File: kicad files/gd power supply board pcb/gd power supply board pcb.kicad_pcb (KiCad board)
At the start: 2 copper layers, 86.9 x 40.1 mm, 129 parts, among them J1 15V_IN, J2 15V_IN, J3 Edge Connector, Q1 FDS9435A, Q2 BC817, Q3 MMBT3906, Q4 FDS9435A, U1 MAX17580, U2 mc34063, U3 TPS563240DDCR, U4 TPS563240DDCR

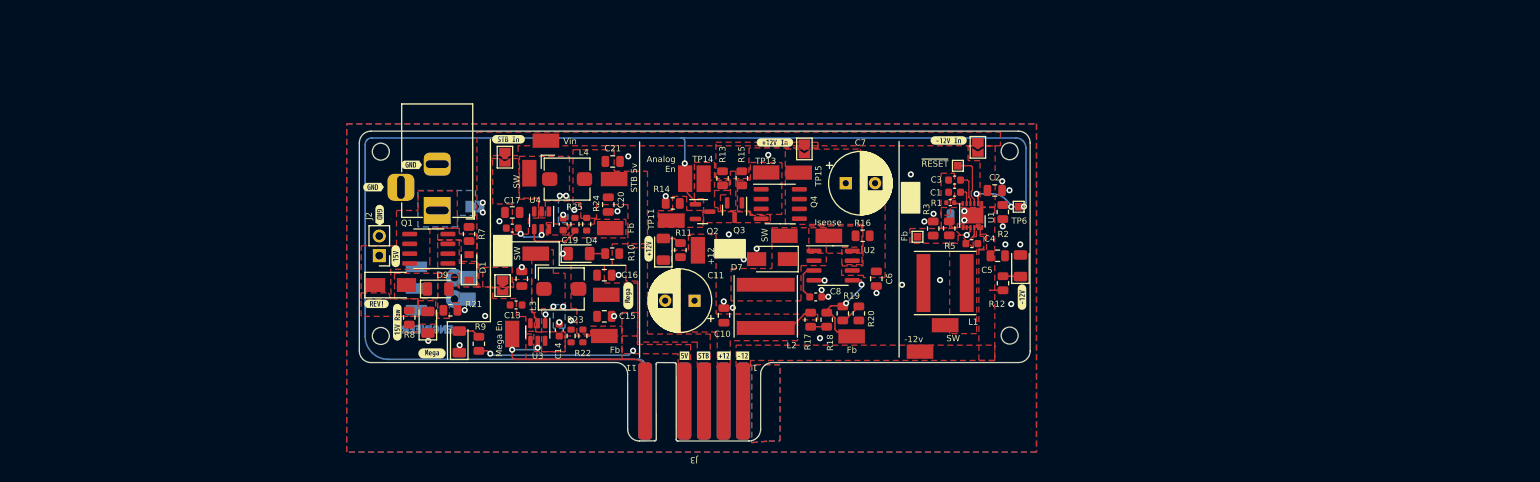
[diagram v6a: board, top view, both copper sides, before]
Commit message: added filters and ripped up the board
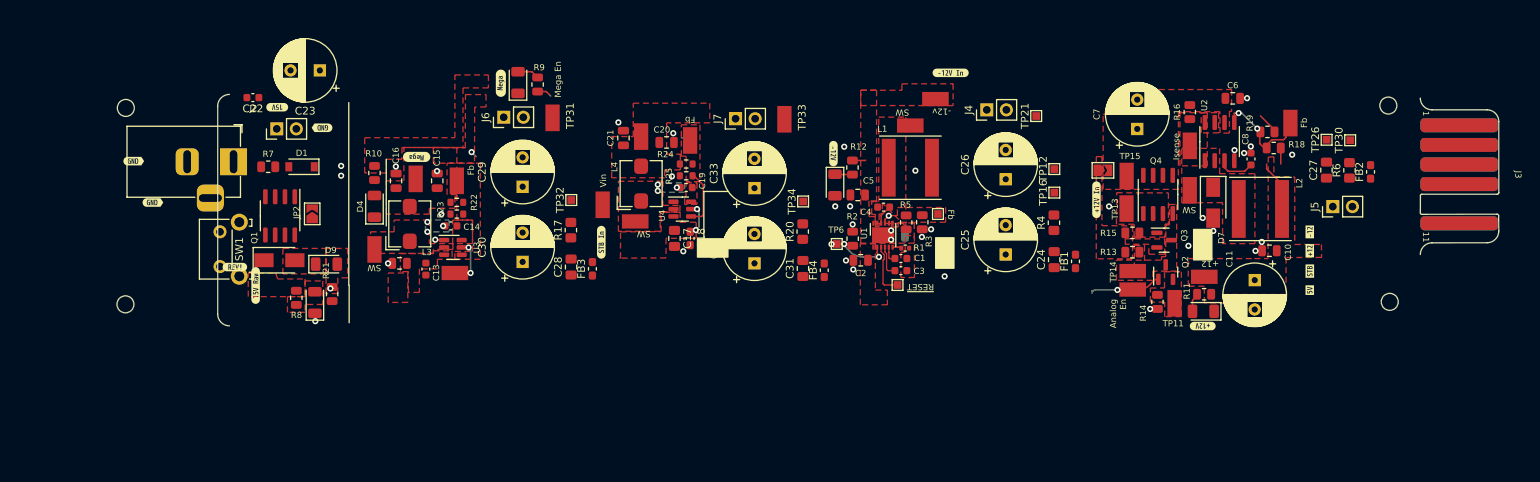
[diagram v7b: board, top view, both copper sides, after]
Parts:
- removed JP3: neg_12_jmp, Jumper:SolderJumper-2_P1.3mm_Open_TrianglePad1.0x1.5mm
- removed JP4: mega_5v_jmp, Jumper:SolderJumper-2_P1.3mm_Open_TrianglePad1.0x1.5mm
- removed JP5: stb_5v_jmp, Jumper:SolderJumper-2_P1.3mm_Open_TrianglePad1.0x1.5mm
- removed REF**: Polarity_Center_Positive_6mm_SilkScreen, Symbol:Polarity_Center_Positive_6mm_SilkScreen
- removed REF**: OSHW-Logo2_7.3x6mm_SilkScreen, Symbol:OSHW-Logo2_7.3x6mm_SilkScreen
- removed REF**: KiCad-Logo2_5mm_SilkScreen, Symbol:KiCad-Logo2_5mm_SilkScreen
- removed svg2mod: G***, My Libraries:BE10v2
- added C22: 1u, Capacitor_SMD:C_0603_1608Metric, F.Cu at (85.8, 74.5)
- added C23: 120u, Capacitor_THT:CP_Radial_D8.0mm_P3.80mm, F.Cu at (94.5, 71.0)
- added C24: Cdamp, Capacitor_SMD:C_0805_2012Metric_Pad1.18x1.45mm_HandSolder, F.Cu at (189.6, 95.5)
- added C25: 120u, Capacitor_THT:CP_Radial_D8.0mm_P3.80mm, F.Cu at (183.3, 94.9)
- added C26: 120u, Capacitor_THT:CP_Radial_D8.0mm_P3.80mm, F.Cu at (183.3, 85.1)
- added C27: Cdamp, Capacitor_SMD:C_0805_2012Metric_Pad1.18x1.45mm_HandSolder, F.Cu at (224.9, 83.9)
- added C28: Cdamp, Capacitor_SMD:C_0805_2012Metric_Pad1.18x1.45mm_HandSolder, F.Cu at (127.0, 96.5)
- added C29: 120u, Capacitor_THT:CP_Radial_D8.0mm_P3.80mm, F.Cu at (120.7, 86.1)
- added C30: 120u, Capacitor_THT:CP_Radial_D8.0mm_P3.80mm, F.Cu at (120.7, 95.8)
- added C31: Cdamp, Capacitor_SMD:C_0805_2012Metric_Pad1.18x1.45mm_HandSolder, F.Cu at (157.0, 96.7)
- added C32: 120u, Capacitor_THT:CP_Radial_D8.0mm_P3.80mm, F.Cu at (150.8, 96.0)
- added C33: 120u, Capacitor_THT:CP_Radial_D8.0mm_P3.80mm, F.Cu at (150.8, 86.3)
- added FB1: 220, Inductor_SMD:L_0603_1608Metric_Pad1.05x0.95mm_HandSolder, F.Cu at (192.3, 95.8)
- added FB2: 220, Inductor_SMD:L_0603_1608Metric_Pad1.05x0.95mm_HandSolder, F.Cu at (230.6, 84.2)
- added FB3: 220, Inductor_SMD:L_0603_1608Metric_Pad1.05x0.95mm_HandSolder, F.Cu at (129.8, 96.7)
- added FB4: 220, Inductor_SMD:L_0603_1608Metric_Pad1.05x0.95mm_HandSolder, F.Cu at (159.8, 96.9)
- added J4: -12v_vin, Connector_PinHeader_2.54mm:PinHeader_1x02_P2.54mm_Vertical, F.Cu at (180.9, 76.1)
- added J5: +12v_vin, Connector_PinHeader_2.54mm:PinHeader_1x02_P2.54mm_Vertical, F.Cu at (225.7, 88.7)
- added J6: mega_vin, Connector_PinHeader_2.54mm:PinHeader_1x02_P2.54mm_Vertical, F.Cu at (118.3, 77.1)
- added J7: stb_vin, Connector_PinHeader_2.54mm:PinHeader_1x02_P2.54mm_Vertical, F.Cu at (148.3, 77.3)
- added R4: Rdamp, Resistor_SMD:R_0805_2012Metric_Pad1.20x1.40mm_HandSolder, F.Cu at (189.6, 90.7)
- added R6: Rdamp, Resistor_SMD:R_0805_2012Metric_Pad1.20x1.40mm_HandSolder, F.Cu at (227.8, 84.0)
- added SW1: SW_SPST, Button_Switch_THT:SW_Tactile_SKHH_Angled, F.Cu at (81.5, 96.4)
- added TP12: TestPoint_Harwin, TestPoint:TestPoint_Pad_1.0x1.0mm, F.Cu at (189.6, 83.8)
- added TP16: TestPoint_Harwin, TestPoint:TestPoint_Pad_1.0x1.0mm, F.Cu at (189.6, 86.8)
- added TP21: TestPoint_Harwin, TestPoint:TestPoint_Pad_1.0x1.0mm, F.Cu at (187.3, 76.9)
- added TP26: TestPoint_Harwin, TestPoint:TestPoint_Pad_1.0x1.0mm, F.Cu at (224.9, 80.0)
- added TP30: TestPoint_Harwin, TestPoint:TestPoint_Pad_1.0x1.0mm, F.Cu at (227.9, 80.1)
- added TP31: TestPoint_Harwin, My Libraries:Harwin-S1751-46-Test-Point, F.Cu at (124.6, 77.2)
- added TP32: TestPoint_Harwin, TestPoint:TestPoint_Pad_1.0x1.0mm, F.Cu at (127.0, 87.8)
- added TP33: TestPoint_Harwin, My Libraries:Harwin-S1751-46-Test-Point, F.Cu at (154.6, 77.3)
- added TP34: TestPoint_Harwin, TestPoint:TestPoint_Pad_1.0x1.0mm, F.Cu at (157.1, 88.0)
- C17: footprint Capacitor_SMD:C_0805_2012Metric -> Capacitor_SMD:C_0805_2012Metric_Pad1.18x1.45mm_HandSolder
- C18: footprint Capacitor_SMD:C_0603_1608Metric -> Capacitor_SMD:C_0603_1608Metric_Pad1.08x0.95mm_HandSolder
- C6: value 100u -> 10u
- JP1: value 15V_Jmp -> Limit_Jmp
- JP2: moved to F.Cu
- R1: value R -> dnp
- R13: value 50k -> 47k
- R14: value 30k -> 33k
- R17, R20: value 0 -> Rdamp; footprint Resistor_SMD:R_0805_2012Metric -> Resistor_SMD:R_0805_2012Metric_Pad1.20x1.40mm_HandSolder
- moved J3 109.7 mm to (247.1, 84.5), turned to -90 degrees
- moved kibuzzard-62380FF5 81.4 mm to (222.7, 99.5), turned to 90 degrees
- moved kibuzzard-62381032 79.3 mm to (222.7, 97.0), turned to 90 degrees
- moved kibuzzard-6238106E 78.6 mm to (217.8, 102.0), turned to 180 degrees
- moved kibuzzard-62381000 77.1 mm to (222.7, 94.4), turned to 90 degrees
- moved kibuzzard-6238101E 75.2 mm to (222.7, 91.9), turned to 90 degrees
- moved C11 72.6 mm to (215.6, 98.2), turned to -90 degrees
- moved kibuzzard-62380E7D 72.5 mm to (208.8, 104.1), turned to 180 degrees
- moved C10 71.1 mm to (217.5, 94.4), turned to 0 degrees
- moved D5 70.4 mm to (208.9, 102.2), turned to 180 degrees
- moved R11 68.1 mm to (209.0, 100.0), turned to 0 degrees
- moved TP11 66.0 mm to (205.2, 101.2), turned to -90 degrees
- moved TP20 65.7 mm to (209.0, 97.7), turned to 180 degrees
- moved L2 65.3 mm to (216.3, 89.0), turned to 0 degrees
- moved R14 64.1 mm to (203.0, 101.0), turned to -90 degrees
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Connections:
- net Net-(C12-Pad1) renamed /mega5v/mega_Vin
- D8 pad 1: /15v_Raw -> /15V_SWd
- JP1 pad 1: /Vin -> /pos12/12v_Vin
- JP2 pad 1: /15v_Raw -> /15V_SWd
- Q1 pad 5: /15v_Raw -> /15V_SWd
- Q1 pad 6: /15v_Raw -> /15V_SWd
- Q1 pad 7: /15v_Raw -> /15V_SWd
- Q1 pad 8: /15v_Raw -> /15V_SWd
- Q3 pad 2: /Vin -> /pos12/12v_Vin
- R13 pad 1: /Vin -> /pos12/12v_Vin
- R15 pad 1: /Vin -> /pos12/12v_Vin
- R17 pad 1: /Pos12_Out -> GND
- R17 pad 2: Net-(R17-Pad2) -> Net-(C28-Pad2)
- R18 pad 1: Net-(R18-Pad1) -> Net-(TP19-Pad1)
- R18 pad 2: Net-(R17-Pad2) -> /Pos12_Out
- R19 pad 1: Net-(R18-Pad1) -> GND
- R19 pad 2: Net-(R19-Pad2) -> Net-(TP19-Pad1)
- R20 pad 2: Net-(R19-Pad2) -> Net-(C31-Pad2)
- R3 pad 1: GND -> /neg12/FB
- R3 pad 2: /neg12/FB -> GND
- R5 pad 1: /neg12/FB -> /Neg12_Out
- R5 pad 2: /Neg12_Out -> /neg12/FB
- R8 pad 2: /15v_Raw -> /15V_SWd
- TP19 pad 1: Net-(R18-Pad1) -> Net-(TP19-Pad1)
- U2 pad 5: Net-(R18-Pad1) -> Net-(TP19-Pad1)
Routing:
- net /Analog_En: track 180.4 -> 18.5 mm
- net /Mega_En: track 29.1 -> 6.32 mm
- net /mega_5v: track 20.5 -> 2.76 mm, vias 2 -> 1
- net Net-(TP19-Pad1): track 0.00 -> 16.5 mm, vias 0 -> 2
- net Net-(R18-Pad1): track 13.7 -> 0.00 mm, vias 2 -> 0
- net Net-(R19-Pad2): track 2.84 -> 0.00 mm
- net Net-(R17-Pad2): track 2.08 -> 0.00 mm
- net /Pos12_Out: track 6.64 -> 8.72 mm
- net Net-(D4-Pad2): track 2.01 -> 0.00 mm
- net GND: vias 39 -> 34
- removed copper zone on B.Cu, net /15v_Raw
- removed copper zone on B.Cu, net GND
- removed copper zone on F.Cu, net GND
- removed copper zone on F.Cu, net Net-(D1-Pad2)
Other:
- board size 86.9 x 40.1 mm -> 165.9 x 30 mm
- copper layers 2 -> 4
- board text removed: "STB 5v"

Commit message: rev2 - round 1
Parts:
- removed TP12, TP16, TP6: TestPoint_Harwin, TestPoint:TestPoint_Pad_1.0x1.0mm
- R2: value 10k -> 10K
- moved H3 89.9 mm to (143.4, 107.7)
- moved H2 89.6 mm to (143.6, 67.2)
- moved FB2 61.9 mm to (168.9, 90.0), turned to 0 degrees
- moved R6 58.2 mm to (170.5, 74.3), turned to -90 degrees
- moved J5 58.0 mm to (168.0, 82.9), turned to 0 degrees
- moved C27 54.7 mm to (170.4, 78.4)
- moved J4 43.5 mm to (143.9, 99.1)
- moved R4 42.7 mm to (148.4, 102.0), turned to 0 degrees
- moved FB4 42.1 mm to (121.7, 79.0), turned to -90 degrees
- moved FB1 41.7 mm to (150.7, 98.1), turned to 0 degrees
- moved R20 41.6 mm to (117.5, 78.9)
- moved C31 41.3 mm to (119.8, 78.9)
- moved TP34 40.4 mm to (116.8, 83.9), turned to 0 degrees
- moved C24 39.4 mm to (150.5, 100.0), turned to 180 degrees
- moved C26 37.4 mm to (146.9, 76.4), turned to 0 degrees
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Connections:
- net /neg12/FB renamed /neg12/-12v_FB
- net /pos12/SW renamed /pos12/+12V_SW
- net Net-(R24-Pad1) renamed /stb_5v/stb_FB
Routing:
- net /Analog_En: track 18.5 -> 0.00 mm, vias 4 -> 0
- net Net-(R18-Pad1): track 16.5 -> 4.17 mm, vias 2 -> 0
- net /Pos12_Out: track 8.72 -> 0.00 mm
- net GND: track 3.06 -> 0.00 mm, vias 34 -> 0
- net Net-(D3-Pad2): track 2.85 -> 0.00 mm
- net /mega_5v: track 2.76 -> 0.00 mm, vias 1 -> 0
- net /Neg12_Out: track 1.71 -> 0.00 mm
- net Net-(C4-Pad2): track 1.50 -> 0.00 mm
- net /Vin: vias 2 -> 0
- added copper zone on F.Cu, net /15V_SWd
- added copper zone on In2.Cu, net /Vin
- removed copper zone on F.Cu, net /15v_Raw
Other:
- board size 165.9 x 30 mm -> 156.2 x 46.8 mm
